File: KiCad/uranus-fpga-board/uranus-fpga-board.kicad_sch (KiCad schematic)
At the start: 1 part, among them U1 XC7K325T-3FFG900E

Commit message: new entry
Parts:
- added U2, U3, U4, U5: (no value), W632GU6NB-11sym:, symbol W632GU6NB-11sym:W632GU6NB-11
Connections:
- net GND: no longer U1.C18 (GND), U1.C28 (GND), U1.C6 (GND), U1.C9 (GND), U1.D15 (GND), U1.D25 (GND), U1.D4 (GND), U1.D8 (GND), U1.D9 (GND), U1.E1 (GND), U1.E12 (GND), U1.E2 (GND), U1.E22 (GND), U1.E6 (GND), U1.E9 (GND), U1.F19 (GND), U1.F29 (GND), U1.F4 (GND), U1.F8 (GND), U1.F9 (GND), U1.G1 (GND), U1.G16 (GND), U1.G2 (GND), U1.G26 (GND), U1.G6 (GND), U1.G9 (GND), U1.H13 (GND), U1.H23 (GND), U1.H4 (GND), U1.H8 (GND), U1.H9 (GND), U1.J1 (GND), U1.J10 (GND), U1.J2 (GND), U1.J20 (GND), U1.J30 (GND), U1.J6 (GND), U1.J9 (GND), U1.K17 (GND), U1.K27 (GND), U1.K4 (GND), U1.K8 (GND), U1.K9 (GND), U1.L1 (GND), U1.L14 (GND), U1.L2 (GND), U1.L24 (GND), U1.L6 (GND), U1.L9 (GND), U1.M12 (GND), U1.M14 (GND), U1.M16 (GND), U1.M18 (GND), U1.M21 (GND), U1.M4 (GND), U1.M8 (GND), U1.M9 (GND), U1.N1 (GND), U1.N11 (GND), U1.N13 (GND), U1.N15 (GND), U1.N17 (GND), U1.N2 (GND), U1.N28 (GND), U1.N6 (GND), U1.N9 (GND), U1.P10 (GND), U1.P12 (GND), U1.P14 (GNDADC_0), U1.P16 (GND), U1.P18 (GND), U1.P25 (GND), U1.P4 (GND), U1.P8 (GND), U1.P9 (GND), U1.R1 (GND), U1.R11 (GND), U1.R13 (GND), U1.R17 (GND), U1.R2 (GND), U1.R22 (GND), U1.R6 (GND), U1.R9 (GND), U1.T10 (GND), U1.T12 (GND), U1.T16 (GND), U1.T18 (GND), U1.T19 (GND), U1.T29 (GND), U1.T4 (GND), U1.T8 (GND), U1.U1 (GND), U1.U11 (GND), U1.U13 (GND), U1.U17 (GND), U1.U2 (GND), U1.U26 (GND), U1.U6 (GND), U1.U9 (GND), U1.V10 (GND), U1.V12 (GND), U1.V14 (GND), U1.V16 (GND), U1.V18 (GND), U1.V23 (GND), U1.V4 (GND), U1.V8 (GND), U1.V9 (GND), U1.W1 (GND), U1.W11 (GND), U1.W13 (GND), U1.W15 (GND), U1.W17 (GND), U1.W2 (GND), U1.W20 (GND), U1.W30 (GND), U1.W6 (GND), U1.W9 (GND), U1.Y17 (GND), U1.Y27 (GND), U1.Y3 (GND), U1.Y4 (GND), U1.Y7 (GND), U1.Y8 (GND), U1.Y9 (GND)
- net at U1.AD12 (IO_L12P_T1_MRCC_33): now also U2.L2 (CS#), U3.L2 (CS#), U4.L2 (CS#), U5.L2 (CS#)
- net at U1.AD16 (IO_L14N_T2_SRCC_32): now also U4.F8 (DQL3)
- net at U1.AD17 (IO_L14P_T2_SRCC_32): now also U4.F2 (DQL2)
- net at U1.AD18 (IO_L13P_T2_MRCC_32): now also U4.E3 (DQL0)
- net at U1.AE11 (IO_L11P_T1_SRCC_33): now also U2.K3 (CAS#), U3.K3 (CAS#), U4.K3 (CAS#), U5.K3 (CAS#)
- net at U1.AE18 (IO_L13N_T2_MRCC_32): now also U4.F7 (DQL1)
- net at U1.AE5 (IO_L11P_T1_SRCC_34): now also U2.A2 (DQU5)
- net at U1.AF11 (IO_L11N_T1_SRCC_33): now also U2.L3 (WE#), U3.L3 (WE#), U4.L3 (WE#), U5.L3 (WE#)
- net at U1.AF17 (IO_L12P_T1_MRCC_32): now also U5.A3 (DQU7)
- net at U1.AF18 (IO_L11P_T1_SRCC_32): now also U5.A2 (DQU5)
- net at U1.AF5 (IO_L11N_T1_SRCC_34): now also U2.B8 (DQU6)
- net at U1.AF6 (IO_L12P_T1_MRCC_34): now also U2.A3 (DQU7)
- net at U1.AG18 (IO_L11N_T1_SRCC_32): now also U5.B8 (DQU6)
- net at U1.AG2 (IO_L15P_T2_DQS_34): now also U3.F3 (DQSL)
- net at U1.AG5 (IO_L12N_T1_MRCC_34): now also U2.T2 (RESET#), U3.T2 (RESET#), U4.T2 (RESET#), U5.T2 (RESET#)
- net at U1.AH1 (IO_L15N_T2_DQS_34): now also U3.G3 (DQSL#)
- net at U1.AH4 (IO_L13P_T2_MRCC_34): now also U3.E3 (DQL0)
- net at U1.AH5 (IO_L14N_T2_SRCC_34): now also U3.F8 (DQL3)
- net at U1.AH6 (IO_L14P_T2_SRCC_34): now also U3.F2 (DQL2)
- net at U1.AJ4 (IO_L13N_T2_MRCC_34): now also U3.F7 (DQL1)
- net at U1.AJ9 (IO_L15P_T2_DQS_33): now also U2.K9 (CKE), U3.K9 (CKE), U4.K9 (CKE), U5.K9 (CKE)
- net at U1.AK9 (IO_L15N_T2_DQS_33): now also U2.K1 (ODT), U3.K1 (ODT), U4.K1 (ODT), U5.K1 (ODT)
- net at U1.Y18 (IO_L15N_T2_DQS_32): now also U4.G3 (DQSL#)
- net at U1.Y19 (IO_L15P_T2_DQS_32): now also U4.F3 (DQSL)
- net at U1.AA10 (IO_L5N_T0_33): now also U1.AA11 (IO_L5P_T0_33), U1.AA12 (IO_L1P_T0_33), U1.AA13 (IO_L6P_T0_33), U1.AA8 (IO_L2P_T0_33), U1.AB12 (IO_L1N_T0_33), U1.AB8 (IO_L2N_T0_33), U1.Y10 (IO_L4N_T0_33), U1.Y11 (IO_L4P_T0_33), U2.L7 (A10/AP), U2.N7 (A12/BC#), U2.P2 (A5), U2.R2 (A7), U2.R3 (A9), U2.R7 (A11), U2.R8 (A6), U2.T3 (A13), U2.T8 (A8), U3.L7 (A10/AP), U3.N7 (A12/BC#), U3.P2 (A5), U3.R2 (A7), U3.R3 (A9), U3.R7 (A11), U3.R8 (A6), U3.T3 (A13), U3.T8 (A8), U4.L7 (A10/AP), U4.N7 (A12/BC#), U4.P2 (A5), U4.R2 (A7), U4.R3 (A9), U4.R7 (A11), U4.R8 (A6), U4.T3 (A13), U4.T8 (A8), U5.L7 (A10/AP), U5.N7 (A12/BC#), U5.P2 (A5), U5.R2 (A7), U5.R3 (A9), U5.R7 (A11), U5.R8 (A6), U5.T3 (A13), U5.T8 (A8)
- net at U1.AB9 (IO_L3P_T0_DQS_33): now also U2.J7 (CK), U3.J7 (CK), U4.J7 (CK), U5.J7 (CK)
- net at U1.AC1 (IO_L2N_T0_34): now also U2.F2 (DQL2)
- net at U1.AC2 (IO_L2P_T0_34): now also U2.F7 (DQL1)
- net at U1.AC4 (IO_L4N_T0_34): now also U2.H3 (DQL4)
- net at U1.AC5 (IO_L4P_T0_34): now also U2.F8 (DQL3)
- net at U1.AC9 (IO_L3N_T0_DQS_33): now also U2.K7 (CK#), U3.K7 (CK#), U4.K7 (CK#), U5.K7 (CK#)
- net at U1.AD1 (IO_L3N_T0_DQS_34): now also U2.G3 (DQSL#)
- net at U1.AD2 (IO_L3P_T0_DQS_34): now also U2.F3 (DQSL)
- net at U1.AD3 (IO_L1N_T0_34): now also U2.E3 (DQL0)
- net at U1.AD4 (IO_L1P_T0_34): now also U2.E7 (DML)
- net at U1.AD6 (IO_L5P_T0_34): now also U2.H8 (DQL5)
- net at U1.AE6 (IO_L5N_T0_34): now also U2.G2 (DQL6)
- net at U1.AF15 (IO_L4P_T0_32): now also U5.F8 (DQL3)
- net at U1.AG14 (IO_L4N_T0_32): now also U5.H3 (DQL4)
- net at U1.AG15 (IO_L2P_T0_32): now also U5.F7 (DQL1)
- net at U1.AH15 (IO_L2N_T0_32): now also U5.F2 (DQL2)
- net at U1.AH16 (IO_L3P_T0_DQS_32): now also U5.F3 (DQSL)
- net at U1.AH17 (IO_L5P_T0_32): now also U5.H8 (DQL5)
- net at U1.AJ16 (IO_L3N_T0_DQS_32): now also U5.G3 (DQSL#)
- net at U1.AJ17 (IO_L5N_T0_32): now also U5.G2 (DQL6)
- net at U1.AK15 (IO_L1N_T0_32): now also U5.E3 (DQL0)
- net at U1.AK16 (IO_L1P_T0_32): now also U5.E7 (DML)
- net at U1.AA15 (IO_L20P_T3_32): now also U4.D7 (DQU0)
- net at U1.AB15 (IO_L20N_T3_32): now also U4.C3 (DQU1)
- net at U1.AB17 (IO_L18P_T2_32): now also U4.H7 (DQL7)
- net at U1.AB18 (IO_L16N_T2_32): now also U4.H3 (DQL4)
- net at U1.AB19 (IO_L17P_T2_32): now also U4.H8 (DQL5)
- net at U1.AC19 (IO_L17N_T2_32): now also U4.G2 (DQL6)
- net at U1.AF7 (IO_L20P_T3_34): now also U3.D7 (DQU0)
- net at U1.AF8 (IO_L19P_T3_34): now also U3.D3 (DMU)
- net at U1.AG7 (IO_L20N_T3_34): now also U3.C3 (DQU1)
- net at U1.AH2 (IO_L16P_T2_34): now also U3.E7 (DML)
- net at U1.AJ1 (IO_L17P_T2_34): now also U1.C18 (GND), U1.C28 (GND), U1.C6 (GND), U1.C9 (GND), U1.D15 (GND), U1.D25 (GND), U1.D4 (GND), U1.D8 (GND), U1.D9 (GND), U1.E1 (GND), U1.E12 (GND), U1.E2 (GND), U1.E22 (GND), U1.E6 (GND), U1.E9 (GND), U1.F19 (GND), U1.F29 (GND), U1.F4 (GND), U1.F8 (GND), U1.F9 (GND), U1.G1 (GND), U1.G16 (GND), U1.G2 (GND), U1.G26 (GND), U1.G6 (GND), U1.G9 (GND), U1.H13 (GND), U1.H23 (GND), U1.H4 (GND), U1.H8 (GND), U1.H9 (GND), U1.J1 (GND), U1.J10 (GND), U1.J2 (GND), U1.J20 (GND), U1.J30 (GND), U1.J6 (GND), U1.J9 (GND), U1.K17 (GND), U1.K27 (GND), U1.K4 (GND), U1.K8 (GND), U1.K9 (GND), U1.L1 (GND), U1.L14 (GND), U1.L2 (GND), U1.L24 (GND), U1.L6 (GND), U1.L9 (GND), U1.M12 (GND), U1.M14 (GND), U1.M16 (GND), U1.M18 (GND), U1.M21 (GND), U1.M4 (GND), U1.M8 (GND), U1.M9 (GND), U1.N1 (GND), U1.N11 (GND), U1.N13 (GND), U1.N15 (GND), U1.N17 (GND), U1.N2 (GND), U1.N28 (GND), U1.N6 (GND), U1.N9 (GND), U1.P10 (GND), U1.P12 (GND), U1.P14 (GNDADC_0), U1.P16 (GND), U1.P18 (GND), U1.P25 (GND), U1.P4 (GND), U1.P8 (GND), U1.P9 (GND), U1.R1 (GND), U1.R11 (GND), U1.R13 (GND), U1.R17 (GND), U1.R2 (GND), U1.R22 (GND), U1.R6 (GND), U1.R9 (GND), U1.T10 (GND), U1.T12 (GND), U1.T16 (GND), U1.T18 (GND), U1.T19 (GND), U1.T29 (GND), U1.T4 (GND), U1.T8 (GND), U1.U1 (GND), U1.U11 (GND), U1.U13 (GND), U1.U17 (GND), U1.U2 (GND), U1.U26 (GND), U1.U6 (GND), U1.U9 (GND), U1.V10 (GND), U1.V12 (GND), U1.V14 (GND), U1.V16 (GND), U1.V18 (GND), U1.V23 (GND), U1.V4 (GND), U1.V8 (GND), U1.V9 (GND), U1.W1 (GND), U1.W11 (GND), U1.W13 (GND), U1.W15 (GND), U1.W17 (GND), U1.W2 (GND), U1.W20 (GND), U1.W30 (GND), U1.W6 (GND), U1.W9 (GND), U1.Y17 (GND), U1.Y27 (GND), U1.Y3 (GND), U1.Y4 (GND), U1.Y7 (GND), U1.Y8 (GND), U1.Y9 (GND), U2.A9 (VSS), U2.B1 (VSSQ), U2.B3 (VSS), U2.B9 (VSSQ), U2.D1 (VSSQ), U2.D8 (VSSQ), U2.E1 (VSS), U2.E2 (VSSQ), U2.E8 (VSSQ), U2.F9 (VSSQ), U2.G1 (VSSQ), U2.G8 (VSS), U2.G9 (VSSQ), U2.J2 (VSS), U2.J8 (VSS), U2.M1 (VSS), U2.M9 (VSS), U2.P1 (VSS), U2.P9 (VSS), U2.T1 (VSS), U2.T9 (VSS), U3.A9 (VSS), U3.B1 (VSSQ), U3.B3 (VSS), U3.B9 (VSSQ), U3.D1 (VSSQ), U3.D8 (VSSQ), U3.E1 (VSS), U3.E2 (VSSQ), U3.E8 (VSSQ), U3.F9 (VSSQ), U3.G1 (VSSQ), U3.G8 (VSS), U3.G9 (VSSQ), U3.H8 (DQL5), U3.J2 (VSS), U3.J8 (VSS), U3.M1 (VSS), U3.M9 (VSS), U3.P1 (VSS), U3.P9 (VSS), U3.T1 (VSS), U3.T9 (VSS), U4.A9 (VSS), U4.B1 (VSSQ), U4.B3 (VSS), U4.B9 (VSSQ), U4.D1 (VSSQ), U4.D8 (VSSQ), U4.E1 (VSS), U4.E2 (VSSQ), U4.E8 (VSSQ), U4.F9 (VSSQ), U4.G1 (VSSQ), U4.G8 (VSS), U4.G9 (VSSQ), U4.J2 (VSS), U4.J8 (VSS), U4.M1 (VSS), U4.M9 (VSS), U4.P1 (VSS), U4.P9 (VSS), U4.T1 (VSS), U4.T9 (VSS), U5.A9 (VSS), U5.B1 (VSSQ), U5.B3 (VSS), U5.B9 (VSSQ), U5.D1 (VSSQ), U5.D8 (VSSQ), U5.E1 (VSS), U5.E2 (VSSQ), U5.E8 (VSSQ), U5.F9 (VSSQ), U5.G1 (VSSQ), U5.G8 (VSS), U5.G9 (VSSQ), U5.J2 (VSS), U5.J8 (VSS), U5.M1 (VSS), U5.M9 (VSS), U5.P1 (VSS), U5.P9 (VSS), U5.T1 (VSS), U5.T9 (VSS)
- net at U1.AJ2 (IO_L16N_T2_34): now also U3.H3 (DQL4)
- net at U1.AJ3 (IO_L18P_T2_34): now also U3.H7 (DQL7)
- net at U1.AK1 (IO_L17N_T2_34): now also U3.G2 (DQL6)
- net at U1.AA16 (IO_L23N_T3_32): now also U4.A2 (DQU5)
- net at U1.AA17 (IO_L23P_T3_32): now also U4.A7 (DQU4)
- net at U1.AC14 (IO_L22P_T3_32): now also U4.C8 (DQU2)
- net at U1.AC15 (IO_L21N_T3_DQS_32): now also U4.B7 (DQSU#)
- net at U1.AC16 (IO_L21P_T3_DQS_32): now also U4.C7 (DQSU)
- net at U1.AD14 (IO_L22N_T3_32): now also U4.C2 (DQU3)
- net at U1.AH7 (IO_L21P_T3_DQS_34): now also U3.C7 (DQSU)
- net at U1.AJ6 (IO_L22P_T3_34): now also U3.C8 (DQU2)
- net at U1.AJ7 (IO_L21N_T3_DQS_34): now also U3.B7 (DQSU#)
- net at U1.AJ8 (IO_L23P_T3_34): now also U3.A7 (DQU4)
- net at U1.AK4 (IO_L24N_T3_34): now also U3.A3 (DQU7)
- net at U1.AK5 (IO_L24P_T3_34): now also U3.B8 (DQU6)
- net at U1.AK6 (IO_L22N_T3_34): now also U3.C2 (DQU3)
- net at U1.AK8 (IO_L23N_T3_34): now also U3.A2 (DQU5)
- net at U1.Y15 (IO_L24N_T3_32): now also U4.A3 (DQU7)
- net at U1.Y16 (IO_L24P_T3_32): now also U4.B8 (DQU6)
- net at U1.AB10 (IO_L7P_T1_33): now also U2.N2 (A3), U3.N2 (A3), U4.N2 (A3), U5.N2 (A3)
- net at U1.AB13 (IO_L6N_T0_VREF_33): now also U2.P8 (A4), U3.P8 (A4), U4.P8 (A4), U5.P8 (A4)
- net at U1.AC10 (IO_L7N_T1_33): now also U2.P3 (A2), U3.P3 (A2), U4.P3 (A2), U5.P3 (A2)
- net at U1.AC11 (IO_L9N_T1_DQS_33): now also U2.N8 (BA1), U3.N8 (BA1), U4.N8 (BA1), U5.N8 (BA1)
- net at U1.AC12 (IO_L9P_T1_DQS_33): now also U2.M3 (BA2), U3.M3 (BA2), U4.M3 (BA2), U5.M3 (BA2)
- net at U1.AC7 (IO_L6P_T0_34): now also U2.H7 (DQL7)
- net at U1.AD19 (IO_L10P_T1_32): now also U5.C2 (DQU3)
- net at U1.AD8 (IO_L8P_T1_33): now also U2.P7 (A1), U3.P7 (A1), U4.P7 (A1), U5.P7 (A1)
- net at U1.AD9 (IO_L10P_T1_33): now also U2.M2 (BA0), U3.M2 (BA0), U4.M2 (BA0), U5.M2 (BA0)
- net at U1.AE1 (IO_L8P_T1_34): now also U2.C3 (DQU1)
- net at U1.AE16 (IO_L6P_T0_32): now also U5.H7 (DQL7)
- net at U1.AE19 (IO_L10N_T1_32): now also U5.A7 (DQU4)
- net at U1.AE3 (IO_L10N_T1_34): now also U2.A7 (DQU4)
- net at U1.AE4 (IO_L10P_T1_34): now also U2.C2 (DQU3)
- net at U1.AE8 (IO_L8N_T1_33): now also U2.N3 (A0), U3.N3 (A0), U4.N3 (A0), U5.N3 (A0)
- net at U1.AE9 (IO_L10N_T1_33): now also U2.J3 (RAS#), U3.J3 (RAS#), U4.J3 (RAS#), U5.J3 (RAS#)
- net at U1.AF1 (IO_L8N_T1_34): now also U2.C8 (DQU2)
- net at U1.AF2 (IO_L7N_T1_34): now also U2.D7 (DQU0)
- net at U1.AF3 (IO_L7P_T1_34): now also U2.D3 (DMU)
- net at U1.AG19 (IO_L8P_T1_32): now also U5.C3 (DQU1)
- net at U1.AG3 (IO_L9N_T1_DQS_34): now also U2.B7 (DQSU#)
- net at U1.AG4 (IO_L9P_T1_DQS_34): now also U2.C7 (DQSU)
- net at U1.AH19 (IO_L8N_T1_32): now also U5.C8 (DQU2)
- net at U1.AJ18 (IO_L9P_T1_DQS_32): now also U5.C7 (DQSU)
- net at U1.AJ19 (IO_L7P_T1_32): now also U5.D3 (DMU)
- net at U1.AK18 (IO_L9N_T1_DQS_32): now also U5.B7 (DQSU#)
- net at U1.AK19 (IO_L7N_T1_32): now also U5.D7 (DQU0)
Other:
- note added: "+"
- note added: "-"
- note added: "1.35V"
- note added: "1/2 VCC"
- note added: "Address Bits"
- note added: "Bank Address Bit"
- note added: "CLK"
- note added: "CMD Encoding"
- note added: "Chip Select"
- note added: "DRAM GND"
- note added: "DRAM Supply"
- note added: "Data Mask"
- note added: "Enable"
- note added: "IO GND"
- note added: "IO Supply"
- note added: "Lower Bits"
- note added: "Lower Data Strobe"
- note added: "Lower Upper"
- note added: "No Connect"
- note added: "Term Calib"
- note added: "Termination"
- note added: "Upper Bits"
- note added: "Upper Data Strobe"
- note added: "VREF Command"
- note added: "VREF IO"
- note added: "Winbond W632GU6NB-11 DDR3L RAM (x4)"
- note added: "clk_ref_n"
- note added: "clk_ref_p"
- note added: "sys_clk_n"
- note added: "sys_clk_p"
- note added: "sys_rst"
- moved on the sheet: U1A, U1B, U1C, U1D, U1E, U1F, U1G, U1H, U1I, U1J, U1K

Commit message: Nicer KiCad
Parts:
- removed U1: XC7K325T-3FFG900E, FFG900XC7K325T_AMD, symbol 2026-10-05_20-13-35:XC7K325T-3FFG900E
- removed U2, U3, U4, U5: (no value), W632GU6NB-11sym:, symbol W632GU6NB-11sym:W632GU6NB-11
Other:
- added sheet FPGA (fpga.kicad_sch)
- added sheet High Speed IO (highspeed.kicad_sch)
- added sheet Misc Peripherals (peripherals.kicad_sch)
- added sheet Power (power.kicad_sch)
- added sheet RAM (ram.kicad_sch)
- note removed: "+"
- note removed: "-"
- note removed: "1.0V"
- note removed: "1.2-3.3V"
- note removed: "1.2V"
- note removed: "1.35V"
- note removed: "1.8V"
- note removed: "1/2 VCC"
- note removed: "ADC Ground. No plan on using, so reg GND"
- note removed: "Active-Low Asynchronous Reset for FPGA Config"
- note removed: "Address Bits"
- note removed: "Analog Power to GTX Transceivers"
- note removed: "Auxiliary Analog Voltage for GTX"
- note removed: "Auxiliary Power Supply"
- note removed: "BRAM Supply"
- note removed: "Bank Address Bit"
- note removed: "CLK"
- note removed: "CMD Encoding"
- note removed: "Chip Select"
- note removed: "Config Bank Voltage Select"
- note removed: "Config Clock"
- note removed: "Cycle Complete Indicator"
- note removed: "DRAM GND"
- note removed: "DRAM Supply"
- note removed: "Data Mask"
- note removed: "Enable"
- note removed: "GTX Receiver Pairs, ordered by Polarity, Rail, then Bank"
- note removed: "GTX Reference Clocks Differential Inputs, Ordered by Line, Polarity, then Bank"
- note removed: "GTX Transmitter Differential Pairs, ordered by Polarity, Line, then Bank"
- note removed: "IO GND"
- note removed: "IO Pins Grouped by Differential Pair, Polarity, any Special Functions, the Bank"
- note removed: "IO Supply"
- note removed: "Init Status"
- note removed: "Lower Bits"
- note removed: "Lower Data Strobe"
- note removed: "Lower Upper"
- note removed: "Mode Select Pins Map Boot Vector"
- note removed: "No Connect"
- note removed: "Primarily VCCO pins and Grounds VCCO provides power to the Banks VCCINT is for the core logic"
- note removed: "Resistor Calibration Circuit Supply"
- note removed: "Single Ended IO Pins"
- note removed: "Term Calib"
- note removed: "Termination"
- note removed: "Termination Voltage for GTX Transceivers"
- note removed: "Test Pins"
- note removed: "Thermal Diode Temp Monitor"
- note removed: "Upper Bits"
- note removed: "Upper Data Strobe"
- note removed: "VREF Command"
- note removed: "VREF IO"
- note removed: "Voltage Reference Negative"
- note removed: "Voltage Reference Positive"
- note removed: "What do you think these are?"
- note removed: "Winbond W632GU6NB-11 DDR3L RAM (x4)"
- note removed: "XADC Analog System Monitor Core Inputs"
- note removed: "Xilinx Kintex-7 XC7K325T-3FFG900E"
- note removed: "clk_ref_n"
- note removed: "clk_ref_p"
- note removed: "sys_clk_n"
- note removed: "sys_clk_p"
- note removed: "sys_rst"

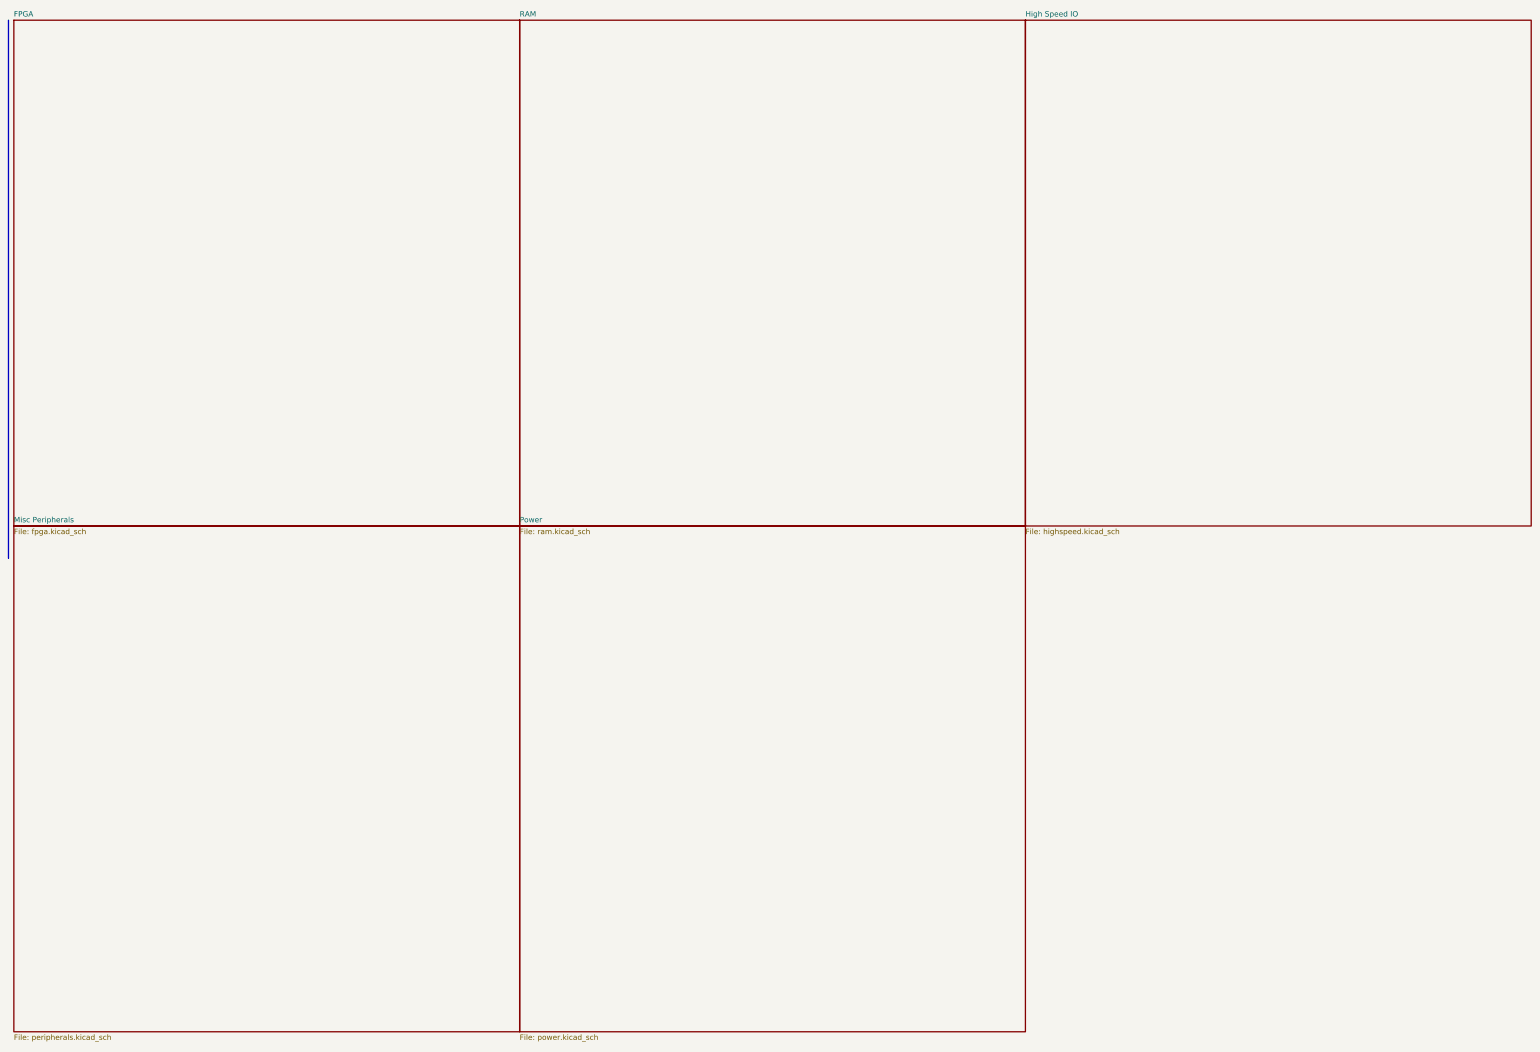
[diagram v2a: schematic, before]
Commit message: updated journal entries and BOM
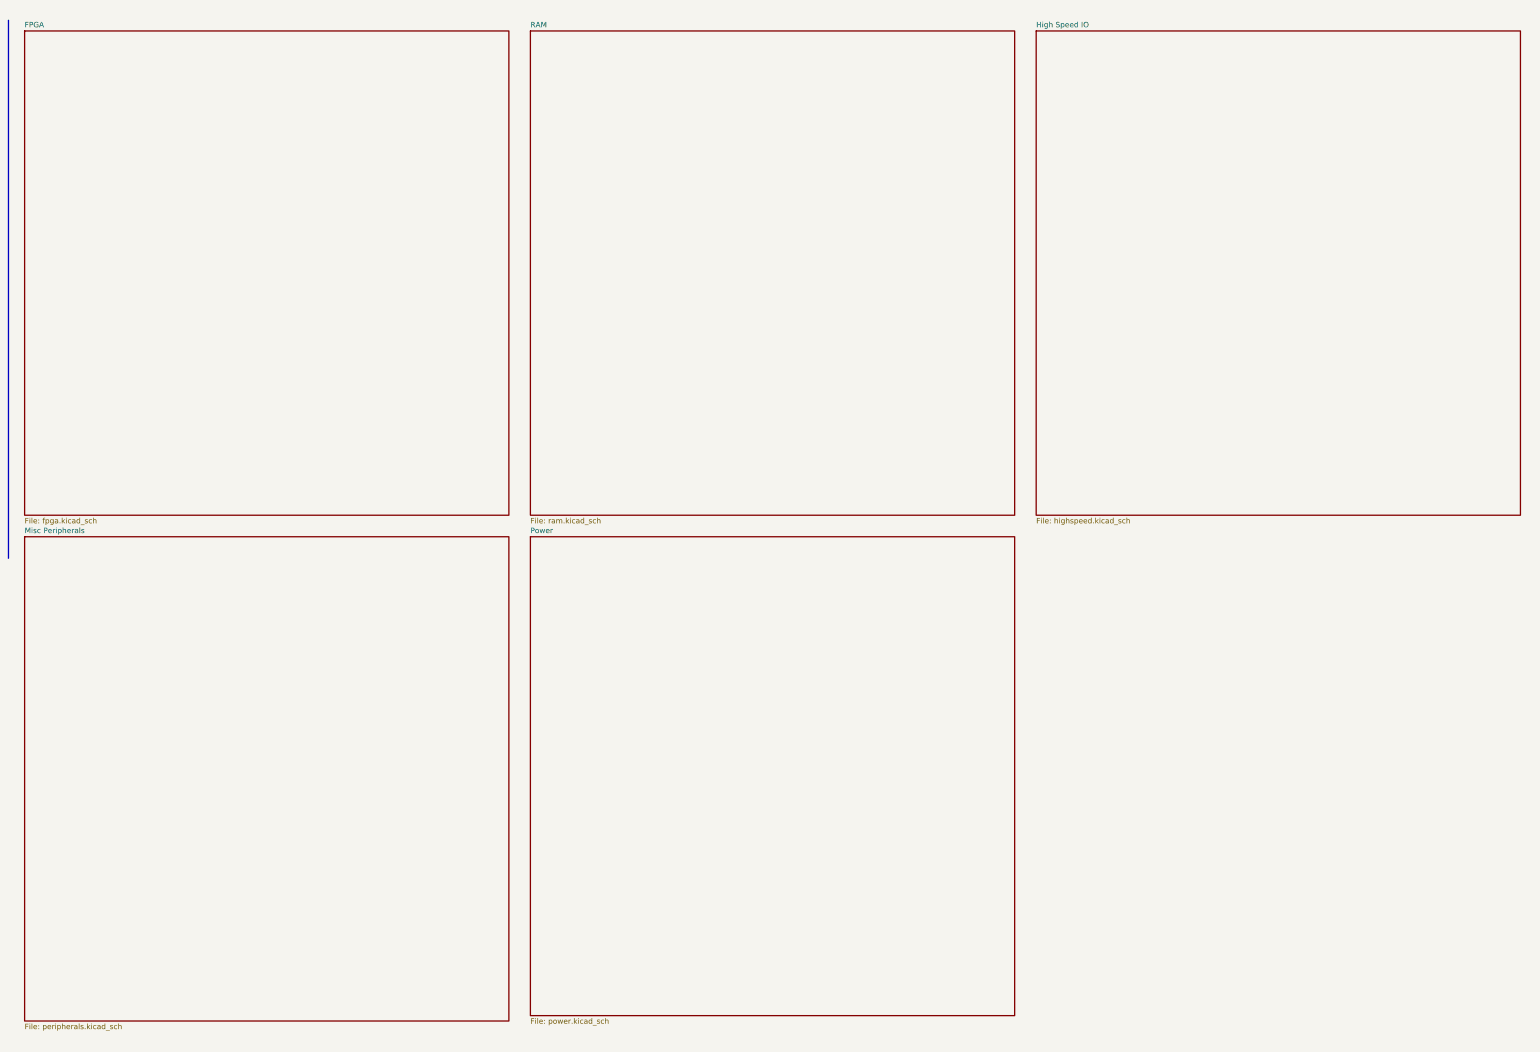
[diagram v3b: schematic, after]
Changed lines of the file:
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@@
 	)
 	(sheet
-		(at 132.08 132.08)
-		(size 119.38 119.38)
+		(at 134.62 134.62)
+		(size 114.3 113.03)
 		(exclude_from_sim no)
 		(in_bom yes)
@@
 		)
 		(property "Sheetname" "Power"
-			(at 132.08 131.3684 0)
+			(at 134.62 133.9084 0)
 			(show_name no)
 			(do_not_autoplace no)
@@
 		)
 		(property "Sheetfile" "power.kicad_sch"
-			(at 132.08 252.0446 0)
+			(at 134.62 248.2346 0)
 			(show_name no)
 			(do_not_autoplace no)
@@
 	)
 	(sheet
-		(at 12.7 12.7)
-		(size 119.38 119.38)
+		(at 15.24 15.24)
+		(size 114.3 114.3)
 		(exclude_from_sim no)
 		(in_bom yes)
@@
 		)
 		(property "Sheetname" "FPGA"
-			(at 12.7 11.9884 0)
+			(at 15.24 14.5284 0)
 			(show_name no)
 			(do_not_autoplace no)
@@
 		)
 		(property "Sheetfile" "fpga.kicad_sch"
-			(at 12.7 132.6646 0)
+			(at 15.24 130.1246 0)
 			(show_name no)
 			(do_not_autoplace no)
@@
 	)
 	(sheet
-		(at 251.46 12.7)
-		(size 119.38 119.38)
+		(at 254 15.24)
+		(size 114.3 114.3)
 		(exclude_from_sim no)
 		(in_bom yes)
@@
 		)
 		(property "Sheetname" "High Speed IO"
-			(at 251.46 11.9884 0)
+			(at 254 14.5284 0)
 			(show_name no)
 			(do_not_autoplace no)
@@
 		)
 		(property "Sheetfile" "highspeed.kicad_sch"
-			(at 251.46 132.6646 0)
+			(at 254 130.1246 0)
 			(show_name no)
 			(do_not_autoplace no)
@@
 	)
 	(sheet
-		(at 132.08 12.7)
-		(size 119.38 119.38)
+		(at 134.62 15.24)
+		(size 114.3 114.3)
 		(exclude_from_sim no)
 		(in_bom yes)
@@
 		)
 		(property "Sheetname" "RAM"
-			(at 132.08 11.9884 0)
+			(at 134.62 14.5284 0)
 			(show_name no)
 			(do_not_autoplace no)
@@
 		)
 		(property "Sheetfile" "ram.kicad_sch"
-			(at 132.08 132.6646 0)
+			(at 134.62 130.1246 0)
 			(show_name no)
 			(do_not_autoplace no)
@@
 	)
 	(sheet
-		(at 12.7 132.08)
-		(size 119.38 119.38)
+		(at 15.24 134.62)
+		(size 114.3 114.3)
 		(exclude_from_sim no)
 		(in_bom yes)
@@
 		)
 		(property "Sheetname" "Misc Peripherals"
-			(at 12.7 131.3684 0)
+			(at 15.24 133.9084 0)
 			(show_name no)
 			(do_not_autoplace no)
@@
 		)
 		(property "Sheetfile" "peripherals.kicad_sch"
-			(at 12.7 252.0446 0)
-			(show_name no)
-			(do_not_autoplace no)
+			(at 15.24 249.5046 0)
+			(show_name no)
+			(do_not_autoplace no)
